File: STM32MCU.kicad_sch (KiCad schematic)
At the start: 4 parts, among them U5 STM32C542CCT6

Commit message: added 48-12V bricks
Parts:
- added PS1, PS2, PS3, PS4: E48SC12030NRFH, E48SC12030NRFH, symbol E48SC12030NRFH:E48SC12030NRFH
- added R11: 10k, E48SC12030NRFH, symbol Device:R_US
- added R12: 22k, E48SC12030NRFH, symbol Device:R_US
- added R13: 33k, E48SC12030NRFH, symbol Device:R_US
- added R14: 4.7k, E48SC12030NRFH, symbol Device:R_US
- added U1: PKU5511ESI, PKU5511ESI:CONV_PKU5511ESI, symbol PKU5511ESI:PKU5511ESI
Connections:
- net 3.3V: now also R14.1
- net GND: now also PS1.12 (ADDR1), PS1.13 (ADDR0), PS1.4 (VOUT(-)), PS1.8 (SIG_GND), PS2.12 (ADDR1), PS2.4 (VOUT(-)), PS2.8 (SIG_GND), PS3.12 (ADDR1), PS3.4 (VOUT(-)), PS3.8 (SIG_GND), PS4.12 (ADDR1), PS4.4 (VOUT(-)), PS4.8 (SIG_GND), R11.1, R12.1, R13.1, U1.4 (-OUT)
- net SCL: now also PS1.11 (CLOCK), PS2.11 (CLOCK), PS3.11 (CLOCK), PS4.11 (CLOCK)
- net SDA: now also PS1.9 (DATA), PS2.9 (DATA), PS3.9 (DATA), PS4.9 (DATA)
- net SMBALERT: now reaches U5.41 (PB5)
- net SMBALERT: now also PS1.10 (SMBALERT), PS2.10 (SMBALERT), PS3.10 (SMBALERT), PS4.10 (SMBALERT), R14.2
- new net: PS4.13 (ADDR0), R13.2
- new net: PS2.13 (ADDR0), R11.2
- new net: PS3.13 (ADDR0), R12.2
- new net 12V: PS1.6 (VOUT(+)), PS2.6 (VOUT(+)), PS3.6 (VOUT(+)), PS4.6 (VOUT(+))
- new net 48V: PS1.1 (VIN(+)), PS2.1 (VIN(+)), PS3.1 (VIN(+)), PS4.1 (VIN(+)), U1.1 (+IN)
- new net 48V_GND: PS1.2 (ON/OFF), PS1.3 (VIN(-)), PS2.2 (ON/OFF), PS2.3 (VIN(-)), PS3.2 (ON/OFF), PS3.3 (VIN(-)), PS4.2 (ON/OFF), PS4.3 (VIN(-)), U1.3 (-IN)
- new net 5.2V: U1.8 (+OUT)
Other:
- note added: "360W Bricks 48V - 12V (4x)"
- note added: "50W Brick 48V - 5.2V"
- moved on the sheet: C6, C7, C8, U5

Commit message: Nick's changes
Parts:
- removed PS1, PS2, PS3, PS4: E48SC12030NRFH, E48SC12030NRFH, symbol E48SC12030NRFH:E48SC12030NRFH
- removed R11: 10k, E48SC12030NRFH, symbol Device:R_US
- removed R12: 22k, E48SC12030NRFH, symbol Device:R_US
- removed R13: 33k, E48SC12030NRFH, symbol Device:R_US
- removed U1: PKU5511ESI, PKU5511ESI:CONV_PKU5511ESI, symbol PKU5511ESI:PKU5511ESI
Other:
- note removed: "360W Bricks 48V - 12V (4x)"
- note removed: "50W Brick 48V - 5.2V"
- moved on the sheet: C6, C7, C8, R14, U5

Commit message: Updated MCU
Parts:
- added C10: 4.7u, symbol Device:C
- added C11, C9: 100n, symbol Device:C
- added C12: 27pF, symbol Device:C
- added C13: 2.2u, symbol Device:C
- added C5: 0.1u, symbol Device:C
- added J7: Conn_02x05_Odd_Even, Oscillator:Oscillator_SMD_ECS_2520MV-xxx-xx-4Pin_2.5x2.0mm, symbol Connector_Generic:Conn_02x05_Odd_Even
- added R10, R11: 4.7k, symbol Device:R_US
- added R12: 10k, Resistor_THT:R_Array_SIP4, symbol Device:R_US
- added SW1: SW_Push, Button_Switch_THT:SW_NKK_GW12LJP, symbol Switch:SW_Push
- added Y1: ECS-120-18-33-JGN-TR, ECS-120-18-33-JGN-TR:XTAL_ECS-120-18-33-JGN-TR, symbol ECS-120-18-33-JGN-TR:ECS-120-18-33-JGN-TR
- C6: value 0.1uF -> 27pF; footprint SOT-23-5_MC_MCH -> (none)
- C7, C8: value 0.1uF -> 100n; footprint SOT-23-5_MC_MCH -> (none)
- renumbered R14 to R13, U5 to U4
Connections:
- net GND: now also U4.8 (VREF-), C10.2, C11.2, C12.2, C13.2, C5.2, C9.2, J7.5 (Pin_5), J7.6 (Pin_6), SW1.1, Y1.2 (GND), Y1.4 (GND__1)
- net SCL: now also R10.1
- net SDA: now also R11.1
- net SWCLK: now also J7.2 (Pin_2)
- net V_CAP: now reaches U4.22 (VCAP)
- net V_CAP: now also C13.1
- net OSC_IN_STM: now reaches U4.5 (PH0-OSC_IN)
- net OSC_IN_STM: now also C6.2, Y1.1 (IN/OUT)
- net OSC_OUT_STM: now reaches U4.6 (PH1-OSC_OUT)
- net OSC_OUT_STM: now also C12.1, Y1.3 (OUT/IN)
- net NRST: now reaches U4.7 (NRST)
- net NRST: now also C5.1, J7.1 (Pin_1), R12.2, SW1.2
- net +3.3V: now reaches U4.9 (VREF+)
- net +3.3V: now also C7.1, C8.1, R13.1, U4.24 (VDD), U4.36 (VDD), U4.48 (VDD), C10.1, C11.1, C9.1, J7.7 (Pin_7), J7.8 (Pin_8), R10.2, R11.2, R12.1
- removed net 3.3V: C6.2, C7.1, C8.1, R13.1, U4.24 (VDD), U4.36 (VDD), U4.48 (VDD)
- net SWDIO renamed SYS_SWDIO
- net SYS_SWDIO: now also J7.4 (Pin_4)
- no-connect marks 0 -> 7
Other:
- note added: "C9 C10 C12 all for VDD_1 2 3. 4.7u parallel with all three VDD cap to ground C14 to VREF+ C16 to VCap"
- note added: "I2C Pull ups"
- note added: "Place Near STM"
- moved on the sheet: U4

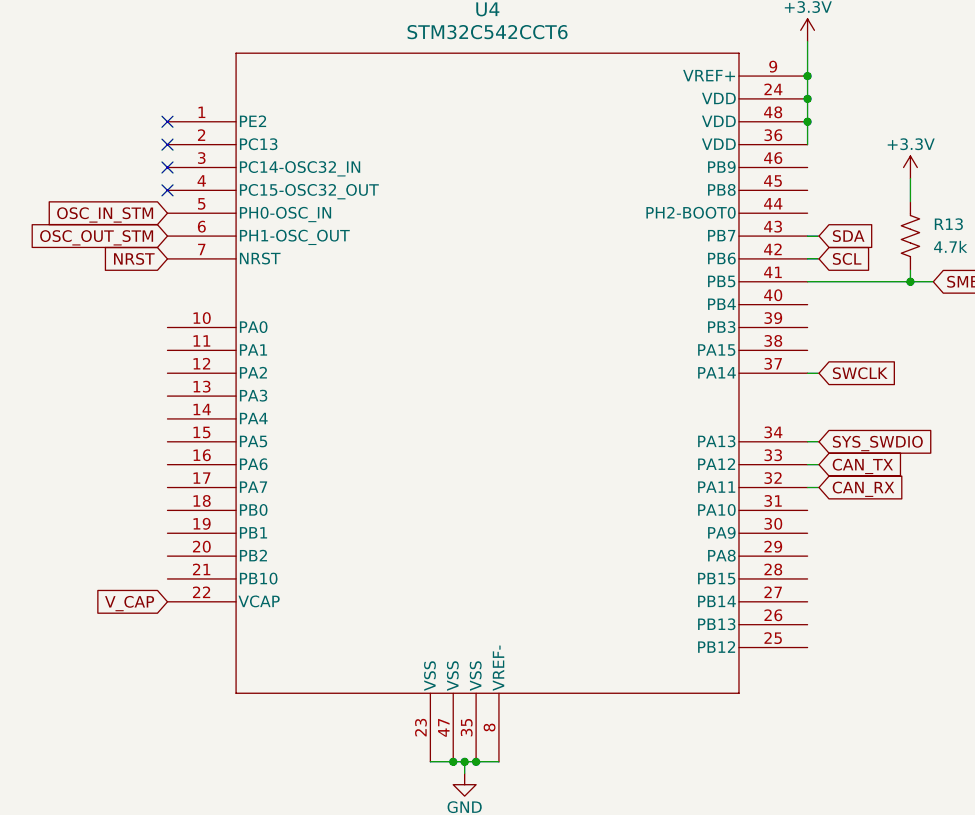
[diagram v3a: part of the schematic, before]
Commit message: fix 48V caps, and add MCU NC
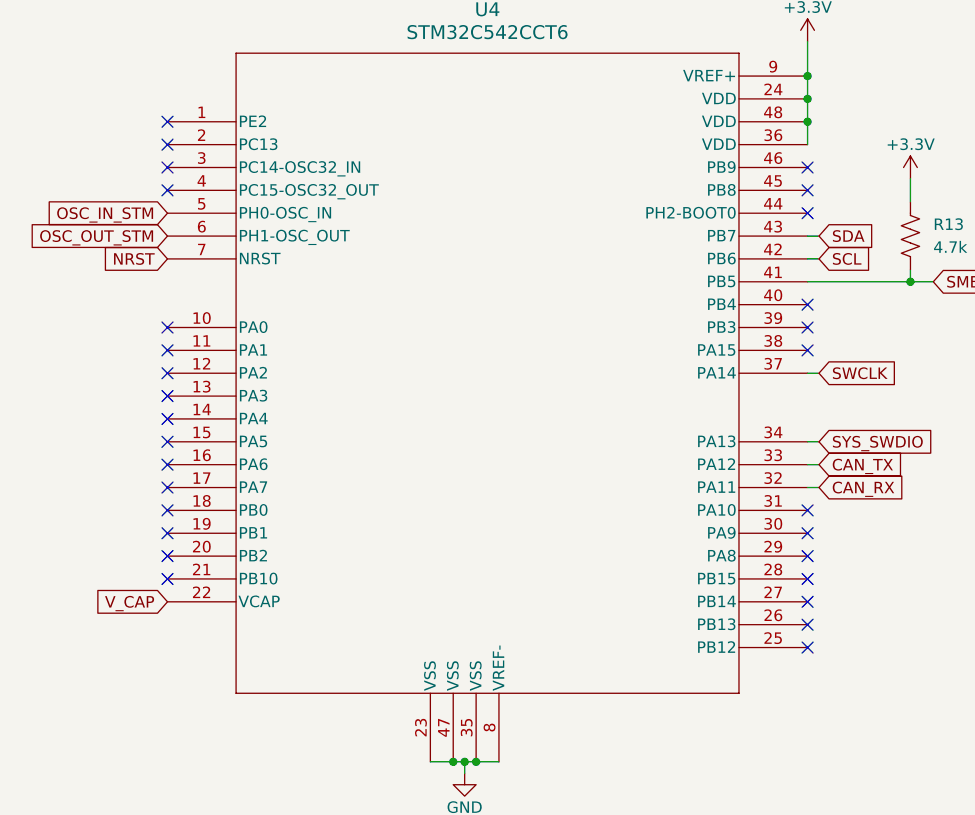
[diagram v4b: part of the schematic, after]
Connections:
- no-connect marks 7 -> 32
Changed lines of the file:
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@@
+	)
+	(no_connect
+		(at 44.45 73.66)
+	)
+	(no_connect
+		(at 115.57 58.42)
 	)
 	(no_connect
 		(at 44.45 43.18)
+	)
+	(no_connect
+		(at 44.45 68.58)
+	)
+	(no_connect
+		(at 44.45 66.04)
+	)
+	(no_connect
+		(at 115.57 91.44)
+	)
+	(no_connect
+		(at 44.45 86.36)
 	)
 	(no_connect
@@
 	)
 	(no_connect
+		(at 115.57 81.28)
+	)
+	(no_connect
+		(at 115.57 45.72)
+	)
+	(no_connect
+		(at 44.45 58.42)
+	)
+	(no_connect
+		(at 115.57 55.88)
+	)
+	(no_connect
+		(at 115.57 40.64)
+	)
+	(no_connect
+		(at 115.57 60.96)
+	)
+	(no_connect
+		(at 44.45 60.96)
+	)
+	(no_connect
+		(at 115.57 86.36)
+	)
+	(no_connect
+		(at 115.57 93.98)
+	)
+	(no_connect
 		(at 190.5 82.55)
 	)
 	(no_connect
+		(at 44.45 83.82)
+	)
+	(no_connect
+		(at 115.57 83.82)
+	)
+	(no_connect
+		(at 44.45 81.28)
+	)
+	(no_connect
+		(at 115.57 43.18)
+	)
+	(no_connect
+		(at 115.57 78.74)
+	)
+	(no_connect
+		(at 115.57 88.9)
+	)
+	(no_connect
+		(at 44.45 71.12)
+	)
+	(no_connect
+		(at 44.45 63.5)
+	)
+	(no_connect
+		(at 44.45 78.74)
+	)
+	(no_connect
+		(at 44.45 76.2)
+	)
+	(no_connect
